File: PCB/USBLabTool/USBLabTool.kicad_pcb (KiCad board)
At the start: 4 copper layers, 79.4 x 56.2 mm, 228 parts, among them J1 Conn_01x06_Pin, J10 T_pwm, J11 T_buf, J12 T_buf, J13 ADC2, J14 ADC1, J15 +3.3VA, J16 +3.3VA, J17 2x01, J19 T_N5V, J2 Conn_02x12_Odd_Even, J20 USB_C_Receptacle, J7 T_amp, J8 T_amp, J9 T_pwm, K1 G5V-2, K2 G5V-2, Q1 STL11N3LLH6, U1 AQY284SX, U10 Opamp_Quad, U11 DG403, U12 STM32H562VGTx, U13 r1283, U14 ST1L05APU33R, U15 ST1L05APU33R, U16 LTC1983ES6-5#TRPBF, U17 TCPP01-M12, U18 74HC245, U2 AQY284SX, U20 74HC245, U3 CD74HC4316PWR, U4 LMP7718, U5 CD74HC4316PWR, U6 LMP7718, U7 OPA863, U8 OPA863, U9 Opamp_Quad, Y1 32.768kHz

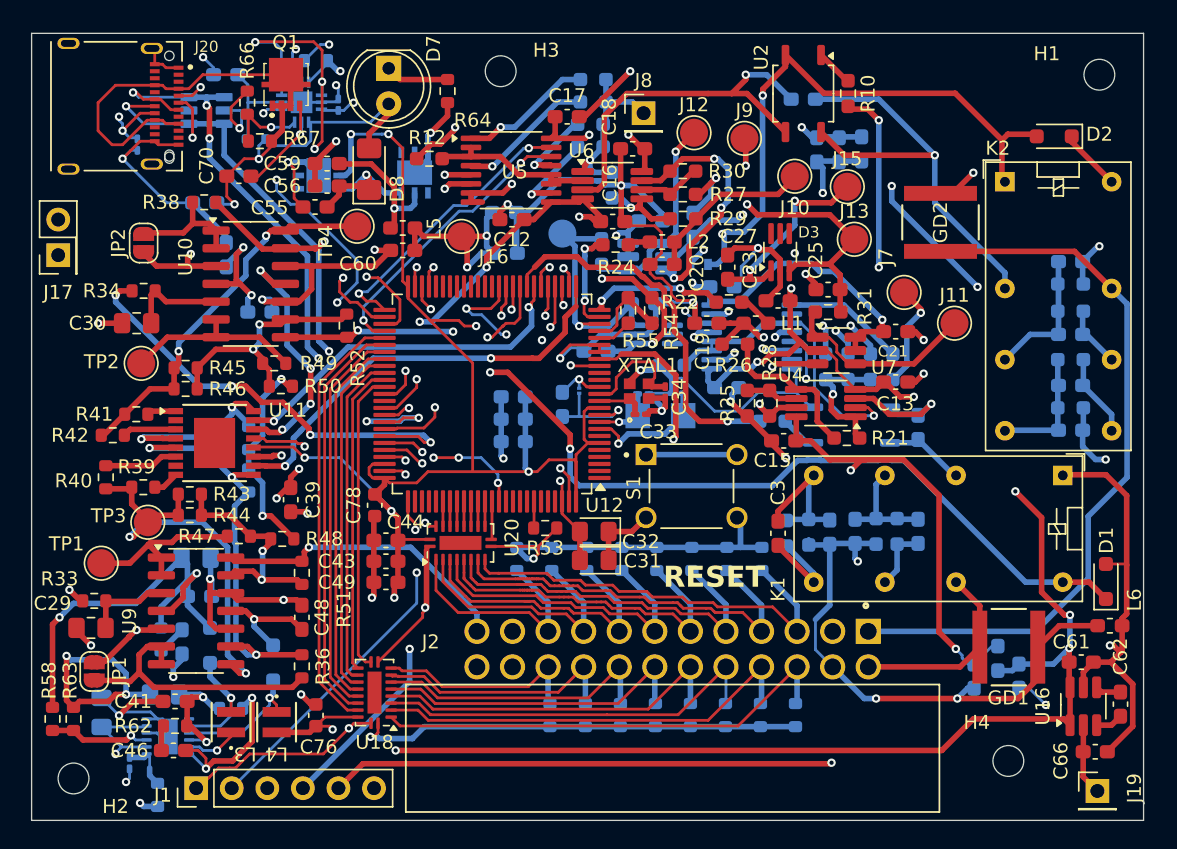
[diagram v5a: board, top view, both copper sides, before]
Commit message: Resolved DRC/ERC errors in PCB and schematic
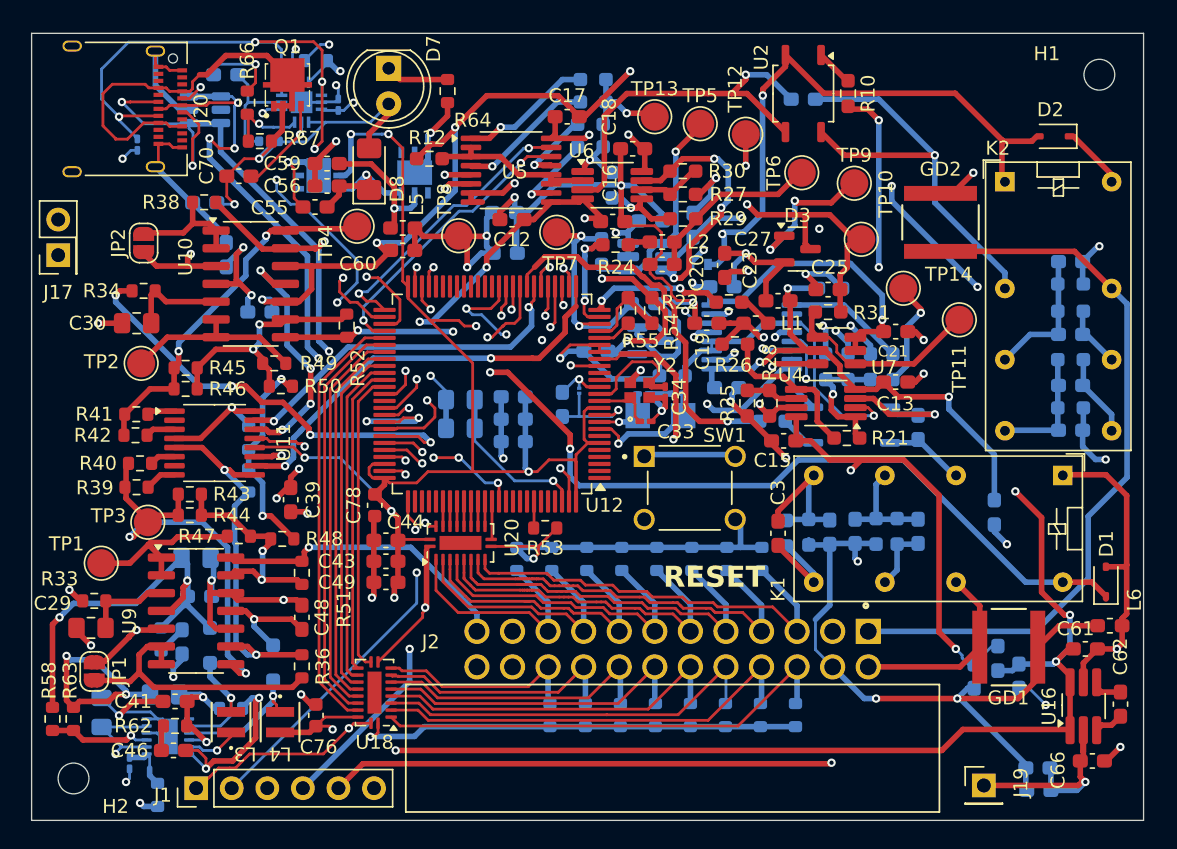
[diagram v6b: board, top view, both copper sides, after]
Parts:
- removed CR1: BAT54KFILM, Diode_SMD:D_SOD-523
- removed H3, H4: MountingHole, MountingHole:MountingHole_2.2mm_M2
- removed J10, J9: T_pwm, TestPoint:TestPoint_Pad_D2.0mm
- removed J11, J12: T_buf, TestPoint:TestPoint_Pad_D2.0mm
- removed J13: ADC2, TestPoint:TestPoint_Pad_D2.0mm
- removed J14: ADC1, TestPoint:TestPoint_Pad_D2.0mm
- removed J15, J16: +3.3VA, TestPoint:TestPoint_Pad_D2.0mm
- removed J7: T_amp, TestPoint:TestPoint_Pad_D2.0mm
- removed J8: T_amp, Connector_PinHeader_2.54mm:PinHeader_1x01_P2.54mm_Vertical
- removed S1: TS02-66-73-BK-100-SCR-D, userfp:SW_TS02-66-73-BK-100-SCR-D
- removed XTAL1: NX2016SA-25M-EXS00A-CS08742, userfp:NX2016SA_NDK
- added L8: 4.7uH, Inductor_SMD:L_0603_1608Metric_Pad1.05x0.95mm_HandSolder, B.Cu at (178.8, 99.8)
- added SW1: TS02-66-73-BK-100-SCR-D, userfp:SW_TS02-66-73-BK-100-SCR-D, F.Cu at (157.0, 98.0)
- added TP10: T_adc_1, TestPoint:TestPoint_Pad_D2.0mm, F.Cu at (169.2, 80.2)
- added TP11: T_buf_1, TestPoint:TestPoint_Pad_D2.0mm, F.Cu at (176.2, 86.0)
- added TP12: T_pwm_1, TestPoint:TestPoint_Pad_D2.0mm, F.Cu at (161.0, 72.8)
- added TP13: T_amp_0, TestPoint:TestPoint_Pad_D2.0mm, F.Cu at (154.5, 71.5)
- added TP14: T_amp_1, TestPoint:TestPoint_Pad_D2.0mm, F.Cu at (172.2, 83.8)
- added TP5: T_buf_0, TestPoint:TestPoint_Pad_D2.0mm, F.Cu at (157.8, 72.0)
- added TP6: T_pwm_0, TestPoint:TestPoint_Pad_D2.0mm, F.Cu at (165.0, 75.5)
- added TP7: T_adc_0, TestPoint:TestPoint_Pad_D2.0mm, F.Cu at (147.5, 79.8)
- added TP8: +3.3VA, TestPoint:TestPoint_Pad_D2.0mm, F.Cu at (140.5, 80.0)
- added TP9: +3.3VA, TestPoint:TestPoint_Pad_D2.0mm, F.Cu at (168.8, 76.2)
- added U19: USBLC6-2SC6, Package_TO_SOT_SMD:SOT-23-6, B.Cu at (122.4, 71.0)
- added Y2: NX2016SA-25M-EXS00A-CS08742, userfp:NX2016SA_NDK, F.Cu at (153.4, 91.0)
- C31, C32: moved to B.Cu
- D1, D2: value 1N4148 -> 1N4148WS; footprint Diode_SMD:D_SOD-323_HandSoldering -> Diode_SMD:D_SOD-323
- D10: value USBLC6-2SC6 -> BAT54KFILM; footprint userfp:SOT95P280X145-6N -> Diode_SMD:D_SOD-523
- D3, D4: value BAV199DW -> BAV99; footprint Package_TO_SOT_SMD:SOT-363_SC-70-6_Handsoldering -> Package_TO_SOT_SMD:SOT-23
- J20: footprint userfp:AMPHENOL_12401832E402A -> Connector_USB:USB_C_Receptacle_Amphenol_12401610E4-2A
- Q1: footprint userfp:STL20N6F7_snapmagic -> userfp:STL20N6F7
- U10, U9: value Opamp_Quad -> MC33274ADR2G
- U11: footprint Package_SO:TSSOP-16-1EP_4.4x5mm_P0.65mm -> Package_SO:TSSOP-16_4.4x5mm_P0.65mm
- U13: value r1283 -> R1283K002A
- U16: value LTC1983ES6-5#TRPBF -> LTC1983ES6-5TRMPBF; footprint Package_TO_SOT_SMD:SOT-23-6_Handsoldering -> Package_TO_SOT_SMD:TSOT-23-6_HandSoldering
- U3, U5: value CD74HC4316PWR -> CD74HC4316
- moved C63 47.9 mm to (181.9, 119.6), turned to 180 degrees
- moved C64 46.0 mm to (181.9, 118.0), turned to 180 degrees
- moved C31 14.9 mm to (140.6, 91.7)
- moved C32 12.1 mm to (140.6, 93.8)
- moved C65 9.93 mm to (167.0, 83.8), turned to 0 degrees
- moved J19 8.12 mm to (178.0, 119.2)
- moved D10 4.96 mm to (127.0, 73.2), turned to 0 degrees
- moved J20 4.10 mm to (115.7, 70.9)
- moved R40 2.64 mm to (117.8, 96.2), turned to 180 degrees
- moved R42 1.62 mm to (117.4, 94.2)
- moved D3 1.25 mm to (164.7, 81.0), turned to 0 degrees
- moved C61 0.99 mm to (185.2, 109.5)
- moved R11 0.76 mm to (155.8, 90.0)
- moved C66 0.69 mm to (185.8, 117.5)
- moved C33 0.61 mm to (153.8, 93.2)
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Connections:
- C11 pad 1: -5V -> -5VCLEAN
- C12 pad 1: -5V -> -5VCLEAN
- C13 pad 1: -5V -> -5VCLEAN
- C16 pad 1: -5V -> -5VCLEAN
- C23 pad 1: -5V -> -5VCLEAN
- C24 pad 1: -5V -> -5VCLEAN
- C31 pad 1: GND -> Net-(C31-Pad1)
- C31 pad 2: VCAP -> Net-(C31-Pad2)
- C32 pad 1: GND -> Net-(C31-Pad1)
- C32 pad 2: VCAP -> Net-(C31-Pad2)
- C65 pad 1: -5V -> -5VCLEAN
- C71 pad 2: Net-(U17-IN_GD) -> Net-(D10-K)
- D10 pad 1: D- -> Net-(D10-K)
- D10 pad 2: GND -> +5V
- GD1 pad 1: P_CH1_IN -> GNDA
- GD1 pad 2: GNDA -> P_CH1_IN
- GD2 pad 1: P_CH0_IN -> GNDA
- GD2 pad 2: GNDA -> P_CH0_IN
- J20 pad A6: D+ -> USB_D+
- J20 pad A7: D- -> USB_D-
- J20 pad B6: D+ -> USB_D+
- J20 pad B7: D- -> USB_D-
- R11 pad 1: GND -> GNDA
- R35 pad 1: -5V -> -5VCLEAN
- R37 pad 1: -5V -> -5VCLEAN
- R48 pad 2: -5V -> -5VCLEAN
- R50 pad 2: -5V -> -5VCLEAN
- U12 pad 48: VCAP -> Net-(C31-Pad2)
- U12 pad 70: D+ -> USB_D-
- U12 pad 71: D- -> USB_D+
- U12 pad 77: DEBUG_JTDI -> unconnected-(U12-PA15(JTDI)-Pad77)
- U12 pad 90: DEBUG_JTRST -> unconnected-(U12-PB4(NJTRST)-Pad90)
- U12 pad 98: VCAP -> Net-(C31-Pad1)
- U17 pad 8: Net-(U17-IN_GD) -> Net-(D10-K)
- U3 pad 9: -5V -> -5VCLEAN
- U4 pad 4: -5V -> -5VCLEAN
- U5 pad 9: -5V -> -5VCLEAN
- U6 pad 4: -5V -> -5VCLEAN
- U7 pad 2: -5V -> -5VCLEAN
- U8 pad 2: -5V -> -5VCLEAN
- Y1 pad 1: RCC_OSC32_IN -> RCC_OSC32_OUT
- Y1 pad 2: RCC_OSC32_OUT -> RCC_OSC32_IN
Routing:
- net -5VCLEAN: track 0.00 -> 108.1 mm, vias 0 -> 9
- net -5V: track 145.8 -> 38.5 mm, vias 10 -> 2
- net USB_D-: track 0.00 -> 50.6 mm, vias 0 -> 4
- net USB_D+: track 0.00 -> 47.9 mm, vias 0 -> 5
- net D+: track 46.2 -> 0.00 mm, vias 4 -> 0
- net D-: track 46.0 -> 0.00 mm, vias 5 -> 0
- net GNDA: track 304.0 -> 331.4 mm, vias 27 -> 26
- net VCAP: track 25.2 -> 0.00 mm, vias 2 -> 0
- net GND: track 294.4 -> 272.4 mm, vias 31 -> 32
- net Net-(C31-Pad1): track 0.00 -> 11.5 mm, vias 0 -> 1
- net Net-(C31-Pad2): track 0.00 -> 10.8 mm, vias 0 -> 2
- net Net-(D10-K): track 0.00 -> 8.43 mm
- net Net-(U17-IN_GD): track 7.38 -> 0.00 mm
- net /AWG_FrontEnd/C1_FB: track 38.4 -> 33.1 mm, vias 3 -> 2
- net UCPD_CC2: track 52.2 -> 55.7 mm, vias 6 -> 5
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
